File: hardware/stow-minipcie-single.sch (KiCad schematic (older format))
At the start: 9 parts, among them P1 mPCIe, U1 SM200, U2 FT232RL

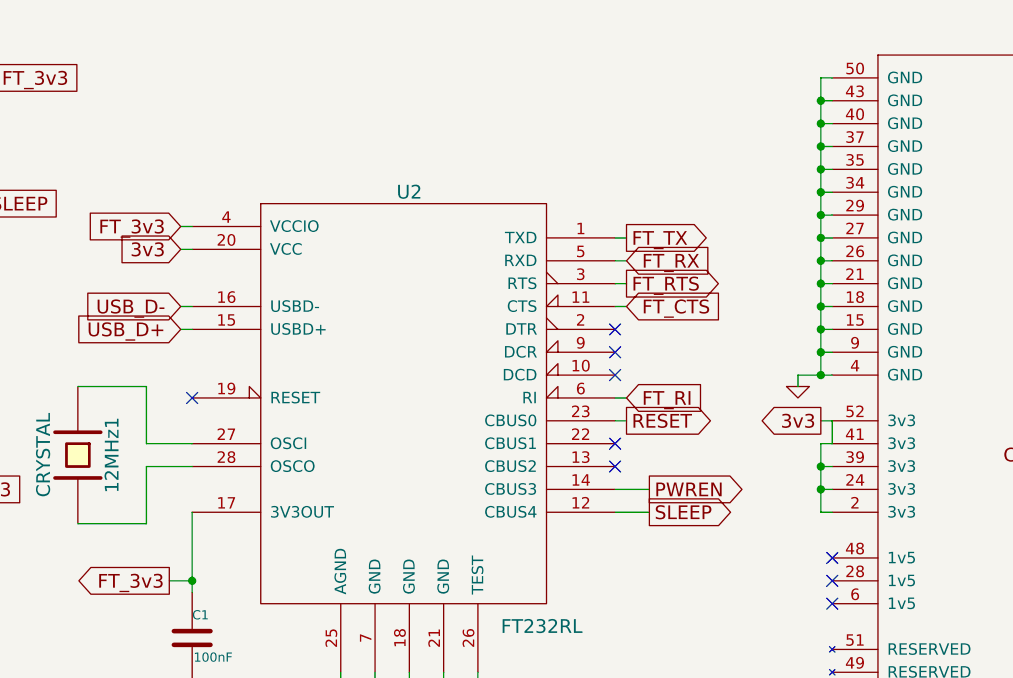
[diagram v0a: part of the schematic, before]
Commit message: Fix a few DRC errors.
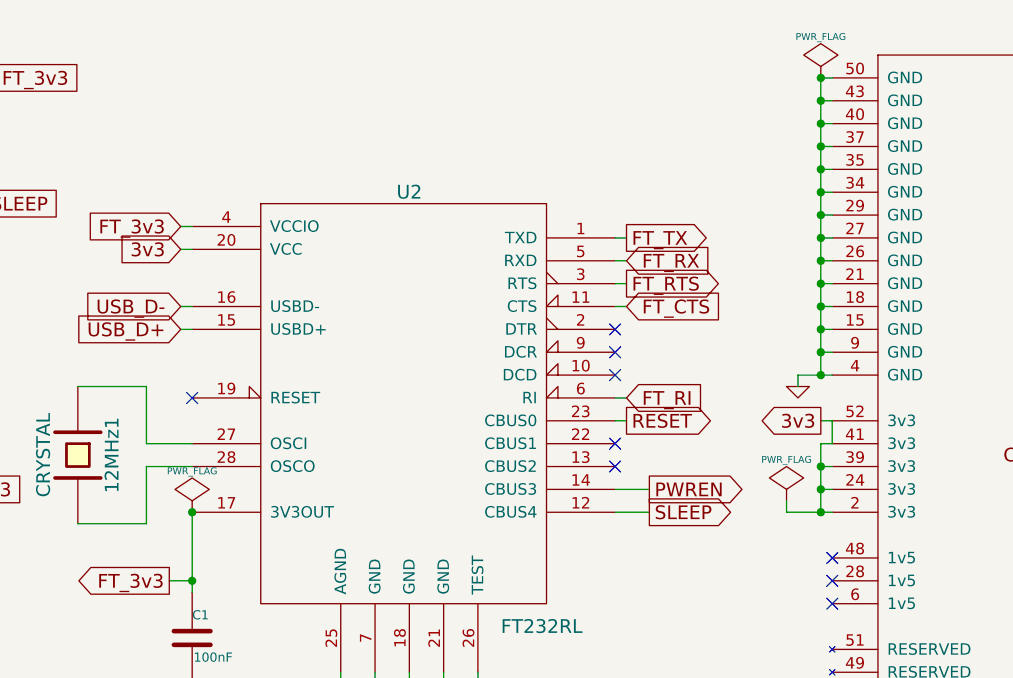
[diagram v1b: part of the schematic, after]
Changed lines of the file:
@@
 Connection ~ 8400 4000
 Wire Wire Line
-	8400 4200 8450 4200
+	8250 4200 8450 4200
 Connection ~ 8400 4100
 Wire Wire Line
@@
 NoConn ~ 3800 5050
 NoConn ~ 3800 5150
+$Comp
+L PWR_FLAG #FLG04
+U 1 1 55FF3712
+P 8400 2300
+F 0 "#FLG04" H 8400 2395 30  0001 C CNN
+F 1 "PWR_FLAG" H 8400 2480 30  0000 C CNN
+F 2 "" H 8400 2300 60  0000 C CNN
+F 3 "" H 8400 2300 60  0000 C CNN
+	1    8400 2300
+	1    0    0    -1
+$EndComp
+Connection ~ 8400 2300
+$Comp
+L PWR_FLAG #FLG05
+U 1 1 55FF3839
+P 8250 4150
+F 0 "#FLG05" H 8250 4245 30  0001 C CNN
+F 1 "PWR_FLAG" H 8250 4330 30  0000 C CNN
+F 2 "" H 8250 4150 60  0000 C CNN
+F 3 "" H 8250 4150 60  0000 C CNN
+	1    8250 4150
+	1    0    0    -1
+$EndComp
+Wire Wire Line
+	8250 4150 8250 4200
+Connection ~ 8400 4200
+$Comp
+L PWR_FLAG #FLG06
+U 1 1 55FF4264
+P 5650 4200
+F 0 "#FLG06" H 5650 4295 30  0001 C CNN
+F 1 "PWR_FLAG" H 5650 4380 30  0000 C CNN
+F 2 "" H 5650 4200 60  0000 C CNN
+F 3 "" H 5650 4200 60  0000 C CNN
+	1    5650 4200
+	1    0    0    -1
+$EndComp
+Connection ~ 5650 4200
 $EndSCHEMATC

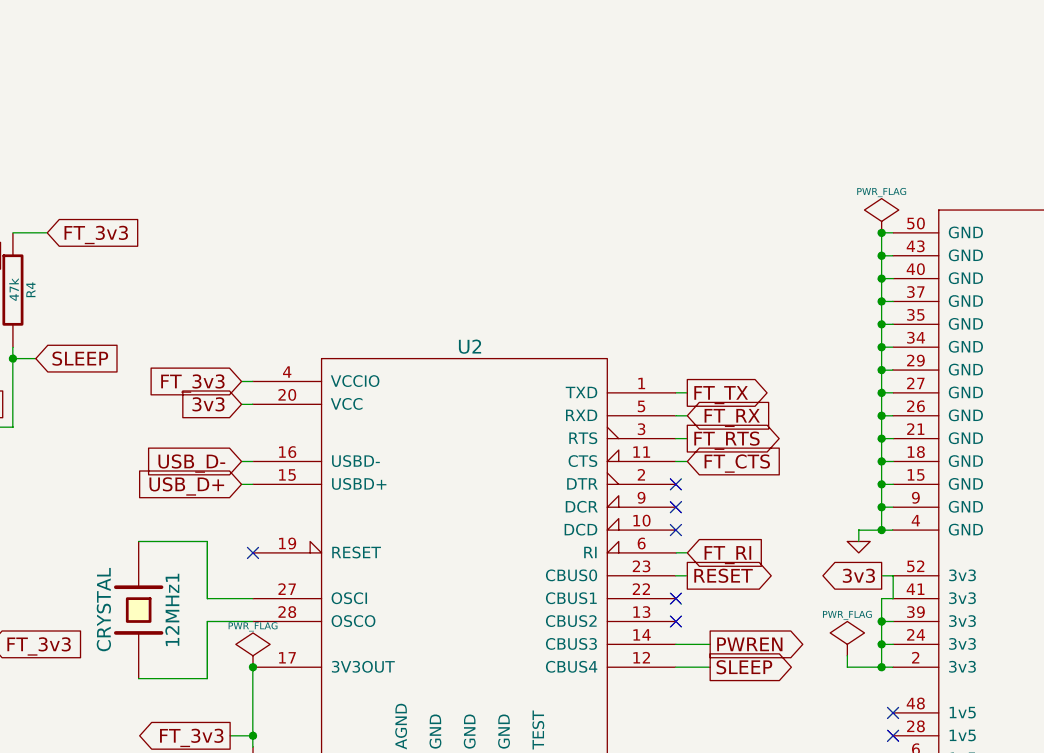
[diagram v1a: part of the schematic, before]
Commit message: Add external USB debugging/programming port.
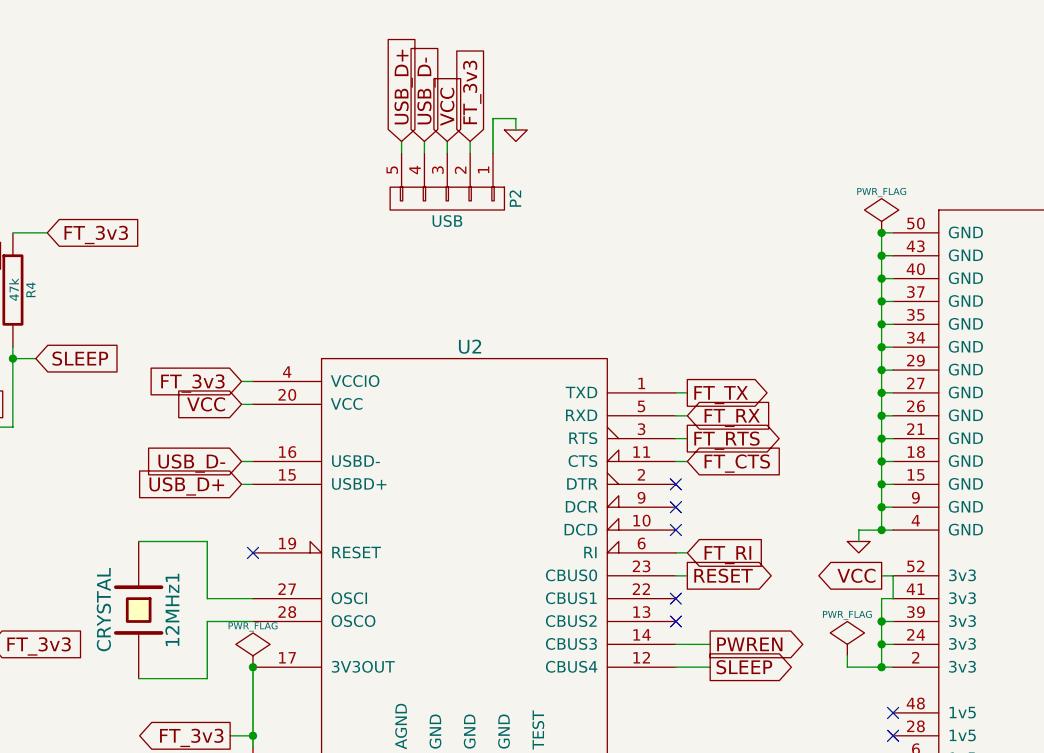
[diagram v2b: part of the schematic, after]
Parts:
- added P2: USB, symbol CONN_01X05
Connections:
- net FT_3v3: now also P2.2 (P2)
- net GND: now also P2.1 (P1)
- net USB_D+: now also P2.5 (P5)
- net USB_D-: now also P2.4 (P4)
- net 3v3 renamed VCC
- net VCC: now also P2.3 (P3)
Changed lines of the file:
@@
 USB_D-
 Text GLabel 5600 3050 0    60   Input ~ 0
-3v3
+VCC
 Text GLabel 8400 3800 0    60   Output ~ 0
-3v3
+VCC
 Text GLabel 2250 3250 0    60   Input ~ 0
 FT_3v3
@@
 $EndComp
 Connection ~ 5650 4200
+$Comp
+L CONN_01X05 P2
+U 1 1 55FF44AF
+P 6500 2150
+F 0 "P2" H 6500 2450 50  0000 C CNN
+F 1 "USB" V 6600 2150 50  0000 C CNN
+F 2 "" H 6500 2150 60  0000 C CNN
+F 3 "" H 6500 2150 60  0000 C CNN
+	1    6500 2150
+	0    1    1    0
+$EndComp
+$Comp
+L GND #PWR07
+U 1 1 55FF454C
+P 6800 1850
+F 0 "#PWR07" H 6800 1850 30  0001 C CNN
+F 1 "GND" H 6800 1780 30  0001 C CNN
+F 2 "" H 6800 1850 60  0000 C CNN
+F 3 "" H 6800 1850 60  0000 C CNN
+	1    6800 1850
+	1    0    0    -1
+$EndComp
+Text GLabel 6500 1900 1    60   Input ~ 0
+VCC
+Text GLabel 6600 1900 1    60   Input ~ 0
+FT_3v3
+Text GLabel 6400 1900 1    60   Input ~ 0
+USB_D-
+Text GLabel 6300 1900 1    60   Input ~ 0
+USB_D+
+Wire Wire Line
+	6800 1850 6800 1800
+Wire Wire Line
+	6800 1800 6700 1800
+Wire Wire Line
+	6700 1800 6700 1950
+Wire Wire Line
+	6600 1900 6600 1950
+Wire Wire Line
+	6500 1950 6500 1900
+Wire Wire Line
+	6400 1900 6400 1950
+Wire Wire Line
+	6300 1950 6300 1900
 $EndSCHEMATC

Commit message: Route the whole board.
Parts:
- 12MHz1: footprint (none) -> Crystals:Crystal_HC49-SD_SMD
- C1: footprint (none) -> Capacitors_SMD:C_0805_HandSoldering
- P1: footprint (none) -> _CrumpPrints:MPCIe_full_card
- P2: footprint (none) -> Pin_Headers:Pin_Header_Straight_1x05
- R1, R2, R3, R4: footprint (none) -> Resistors_SMD:R_0805_HandSoldering
- U1: footprint (none) -> _CrumpPrints:SM200
- U2: footprint (none) -> Housings_SSOP:SSOP-28_5.3x10.2mm_Pitch0.65mm
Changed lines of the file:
@@
 F 0 "U1" H 3050 5500 60  0000 C CNN
 F 1 "SM200" H 3050 1650 60  0000 C CNN
-F 2 "" H 3750 5050 60  0000 C CNN
+F 2 "_CrumpPrints:SM200" H 3750 5050 60  0001 C CNN
 F 3 "" H 3750 5050 60  0000 C CNN
 	1    3050 3800
@@
 F 0 "P1" H 9350 4900 60  0000 C CNN
 F 1 "mPCIe" H 9350 1500 60  0000 C CNN
-F 2 "" H 9350 3500 60  0000 C CNN
+F 2 "_CrumpPrints:MPCIe_full_card" H 9350 3500 60  0001 C CNN
 F 3 "" H 9350 3500 60  0000 C CNN
 	1    9350 3500
@@
 F 0 "U2" H 6600 4600 60  0000 C CNN
 F 1 "FT232RL" H 7000 2700 60  0000 L CNN
-F 2 "" H 6600 3700 60  0000 C CNN
+F 2 "Housings_SSOP:SSOP-28_5.3x10.2mm_Pitch0.65mm" H 6600 3700 60  0001 C CNN
 F 3 "" H 6600 3700 60  0000 C CNN
 	1    6600 3700
@@
 F 0 "R3" V 4430 4350 40  0000 C CNN
 F 1 "10k" V 4357 4351 40  0000 C CNN
-F 2 "" V 4280 4350 30  0000 C CNN
+F 2 "Resistors_SMD:R_0805_HandSoldering" V 4280 4350 30  0001 C CNN
 F 3 "" H 4350 4350 30  0000 C CNN
 	1    4350 4350
@@
 F 0 "R1" V 2030 3650 40  0000 C CNN
 F 1 "10k" V 1957 3651 40  0000 C CNN
-F 2 "" V 1880 3650 30  0000 C CNN
+F 2 "Resistors_SMD:R_0805_HandSoldering" V 1880 3650 30  0001 C CNN
 F 3 "" H 1950 3650 30  0000 C CNN
 	1    1950 3650
@@
 F 0 "R2" V 4130 2750 40  0000 C CNN
 F 1 "10k" V 4057 2751 40  0000 C CNN
-F 2 "" V 3980 2750 30  0000 C CNN
+F 2 "Resistors_SMD:R_0805_HandSoldering" V 3980 2750 30  0001 C CNN
 F 3 "" H 4050 2750 30  0000 C CNN
 	1    4050 2750
@@
 F 0 "R4" V 4680 2550 40  0000 C CNN
 F 1 "47k" V 4607 2551 40  0000 C CNN
-F 2 "" V 4530 2550 30  0000 C CNN
+F 2 "Resistors_SMD:R_0805_HandSoldering" V 4530 2550 30  0001 C CNN
 F 3 "" H 4600 2550 30  0000 C CNN
 	1    4600 2550
@@
 F 0 "12MHz1" H 5150 4100 60  0000 C CNN
 F 1 "CRYSTAL" H 5150 3800 60  0000 C CNN
-F 2 "" H 5150 3950 60  0000 C CNN
+F 2 "Crystals:Crystal_HC49-SD_SMD" H 5150 3950 60  0001 C CNN
 F 3 "" H 5150 3950 60  0000 C CNN
 	1    5150 3950
@@
 F 0 "C1" H 5650 4850 40  0000 L CNN
 F 1 "100nF" H 5656 4665 40  0000 L CNN
-F 2 "" H 5688 4600 30  0000 C CNN
+F 2 "Capacitors_SMD:C_0805_HandSoldering" H 5688 4600 30  0001 C CNN
 F 3 "" H 5650 4750 60  0000 C CNN
 	1    5650 4750
@@
 F 0 "P2" H 6500 2450 50  0000 C CNN
 F 1 "USB" V 6600 2150 50  0000 C CNN
-F 2 "" H 6500 2150 60  0000 C CNN
+F 2 "Pin_Headers:Pin_Header_Straight_1x05" H 6500 2150 60  0001 C CNN
 F 3 "" H 6500 2150 60  0000 C CNN
 	1    6500 2150
@@
 Wire Wire Line
 	6300 1950 6300 1900
+Connection ~ 5150 4250
+Connection ~ 5150 3650
 $EndSCHEMATC
